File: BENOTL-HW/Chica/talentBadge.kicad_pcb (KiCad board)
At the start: 2 copper layers, 96.6 x 102.2 mm, 67 parts, among them P1 USB_A, P2 OLED, P3 Batt, P4 PS, Q1 MMBT3904, Q2 MMBT3904, Q3 IR phototransistor, SW1 B1, SW2 B2, SW3 RST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

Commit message: Gerbers
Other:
- board text added: "Hack me! in: https://goo.gl/GZqPbb"
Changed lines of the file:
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@@
-(kicad_pcb (version 4) (host pcbnew 4.0.7-e2-6376~58~ubuntu16.04.1)
+(kicad_pcb (version 4) (host pcbnew 4.0.7)
   (general
     (links 156)
@@
     (area 109.254274 32.333723 206.347762 148.618677)
     (thickness 1.6)
-    (drawings 6)
+    (drawings 7)
     (tracks 680)
     (zones 0)
@@
   (page A4)
   (layers
-    (0 F.Cu signal)
-    (31 B.Cu signal)
+    (0 F.Cu signal hide)
+    (31 B.Cu signal hide)
     (32 B.Adhes user)
     (33 F.Adhes user)
@@
     (35 F.Paste user)
     (36 B.SilkS user)
-    (37 F.SilkS user)
+    (37 F.SilkS user hide)
     (38 B.Mask user)
     (39 F.Mask user)
@@
     (visible_elements FFFFFFFF)
     (pcbplotparams
-      (layerselection 0x00030_80000001)
-      (usegerberextensions false)
+      (layerselection 0x03fff_80000001)
+      (usegerberextensions true)
       (excludeedgelayer true)
       (linewidth 0.100000)
@@
       (outputformat 1)
       (mirror false)
-      (drillshape 1)
+      (drillshape 0)
       (scaleselection 1)
-      (outputdirectory ""))
+      (outputdirectory Gerbers_Chica/))
   )
   (net 0 "")
@@
     )
   )
+  (gr_text "Hack me! in:\nhttps://goo.gl/GZqPbb" (at 126.94 46.01) (layer B.SilkS)
+    (effects (font (size 1.5 1.5) (thickness 0.3)) (justify mirror))
+  )
   (gr_text SDA (at 160.2 117.6) (layer B.SilkS)

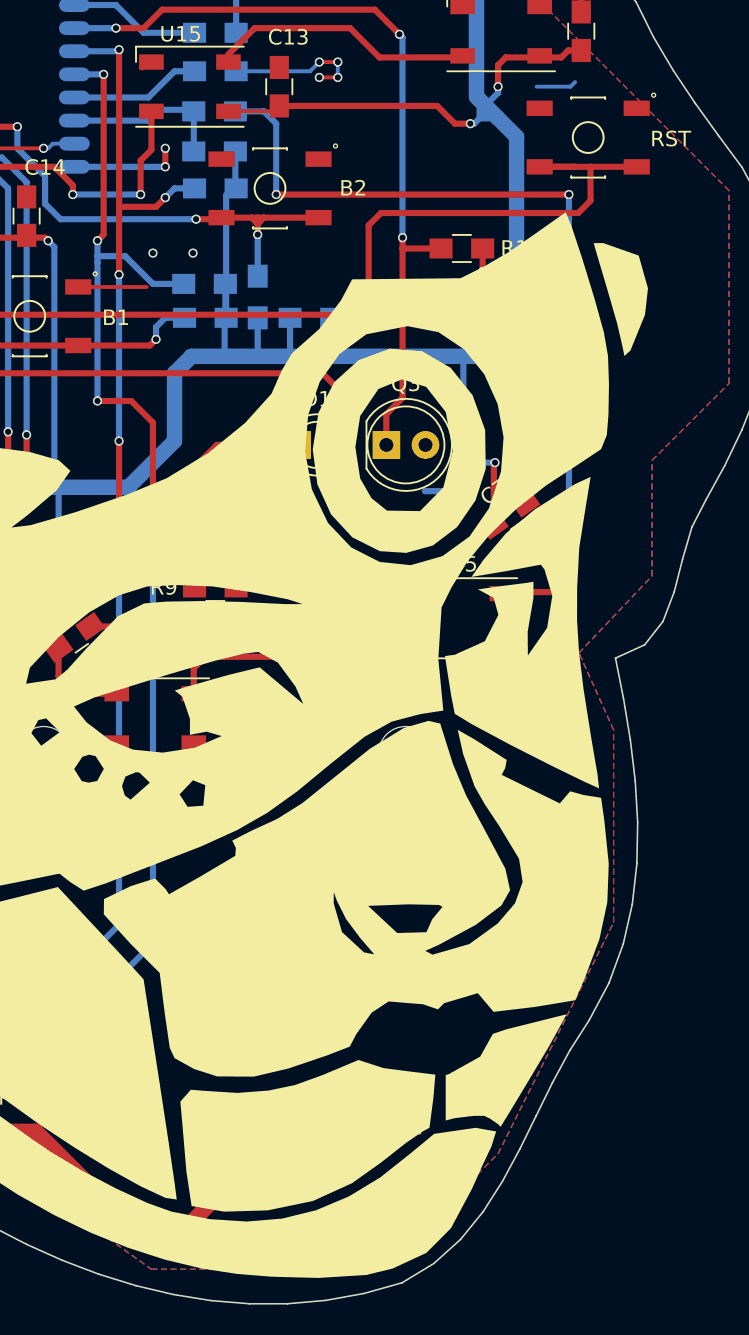
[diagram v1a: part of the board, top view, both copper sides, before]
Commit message: Fix Battery footprint
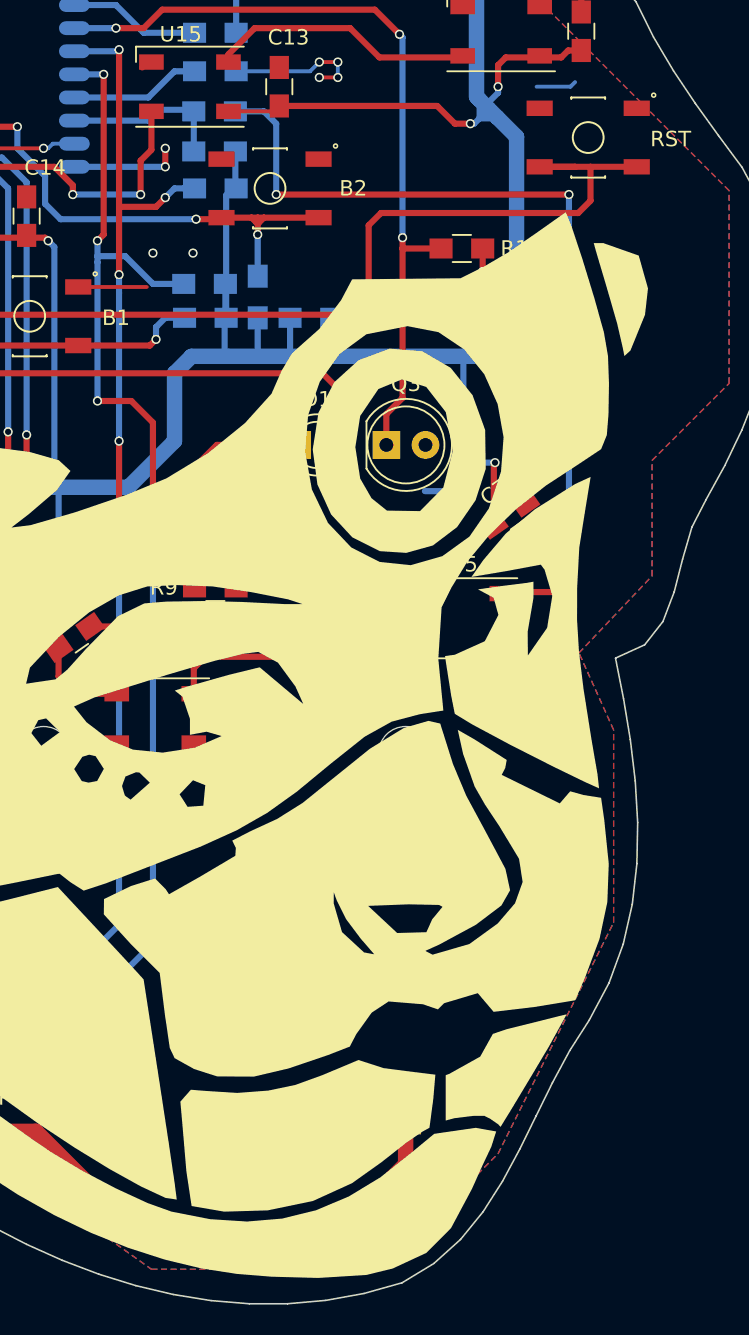
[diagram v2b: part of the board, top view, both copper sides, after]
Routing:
- net Net-(C3-Pad1): track 108.2 -> 123.9 mm
